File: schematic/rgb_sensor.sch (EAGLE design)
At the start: 6 parts, among them IC2 MEGA8-P

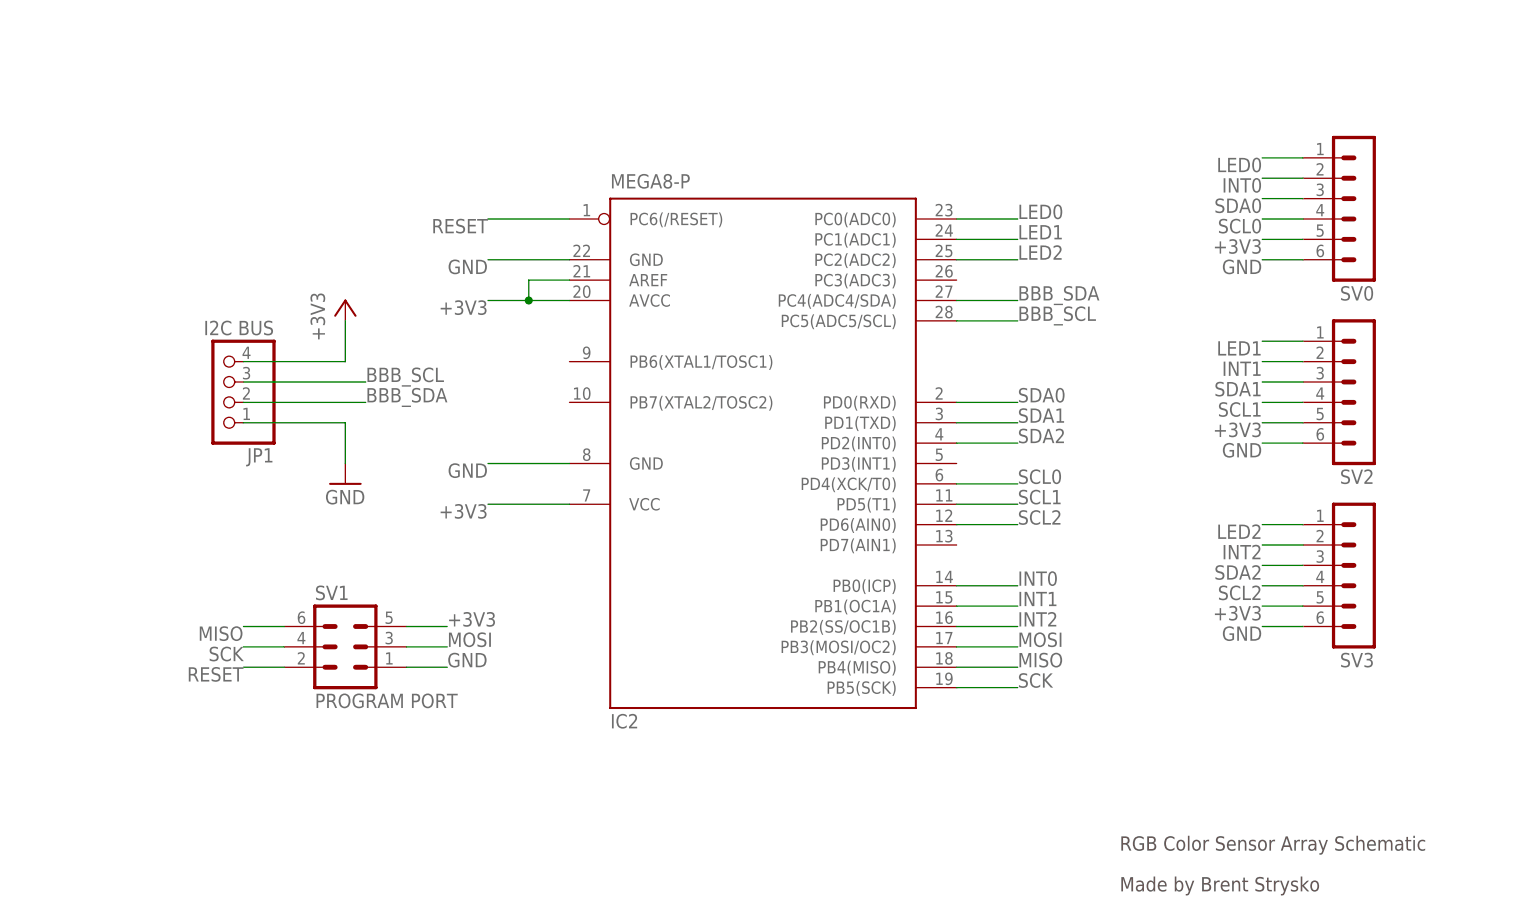
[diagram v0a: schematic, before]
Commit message: Redesigned schematic and board.  Added decoupling capacitors, pullup resistor on reset, and shrunk board size
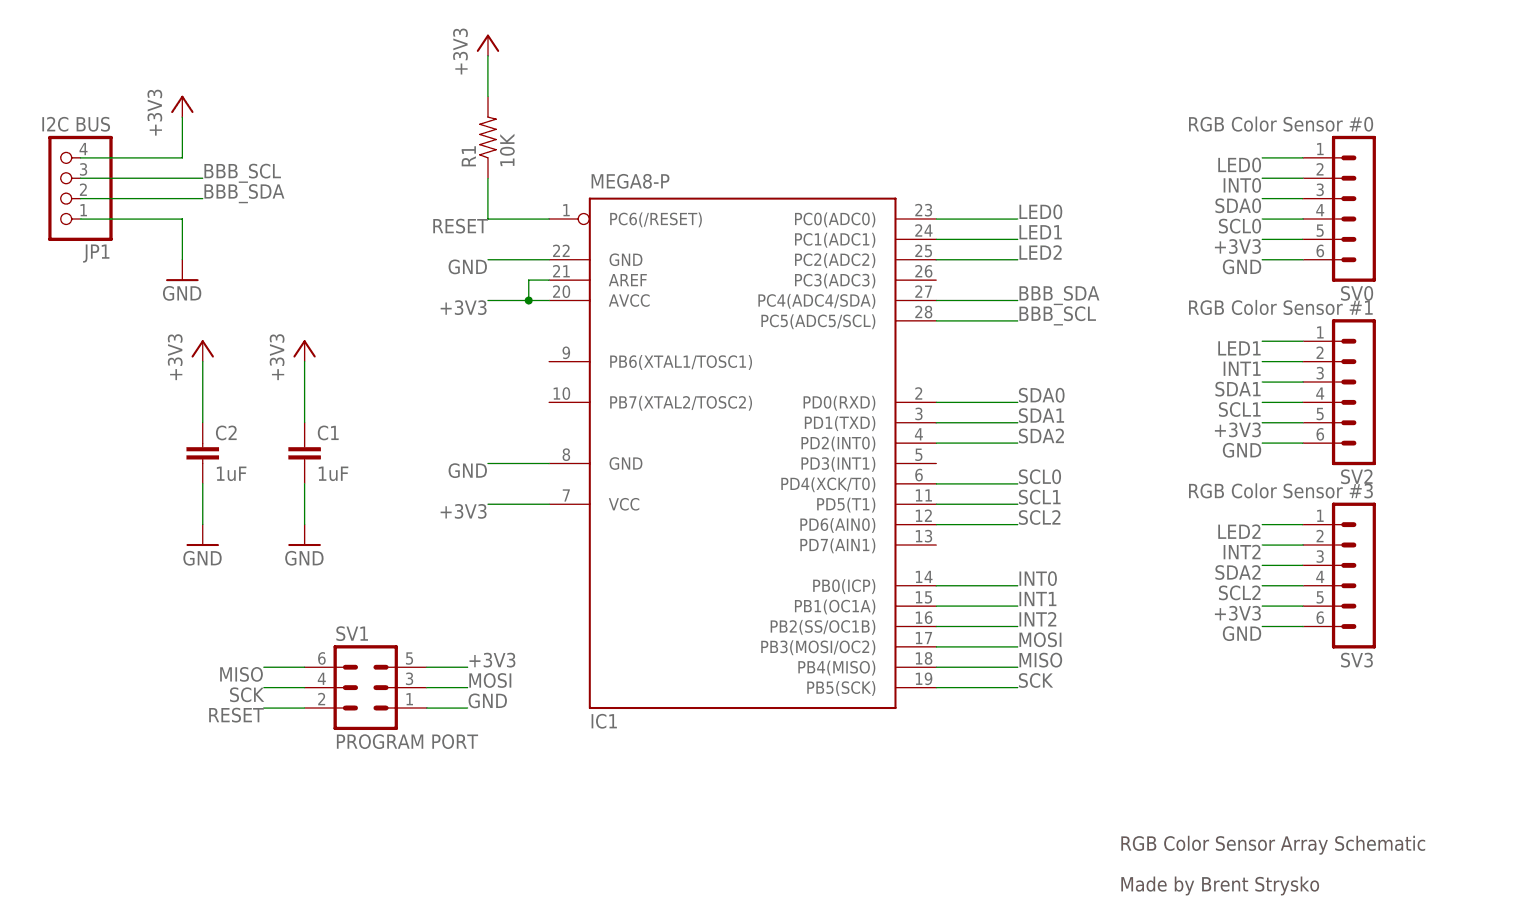
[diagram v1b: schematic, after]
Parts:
- removed IC2: MEGA8-P, atmel:MEGA8-P
- added C1, C2: 1uF, SparkFun-Passives:CAPKIT
- added IC1: MEGA8-P, atmel:MEGA8-P
- added R1: 10K, SparkFun-Passives:RESISTORPTH-1/4W
- SV0: value (none) -> RGB Color Sensor #0
- SV2: value (none) -> RGB Color Sensor #1
- SV3: value (none) -> RGB Color Sensor #3
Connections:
- net +3V3: now also C1.1, C2.1, IC1.AREF, IC1.AVCC, IC1.VCC@1, R1.2; no longer IC2.AREF, IC2.AVCC, IC2.VCC@1
- net BBB_SCL: now also IC1.PC5(ADC5/SCL); no longer IC2.PC5(ADC5/SCL)
- net BBB_SDA: now also IC1.PC4(ADC4/SDA); no longer IC2.PC4(ADC4/SDA)
- net GND: now also C1.2, C2.2, IC1.GND, IC1.GND@1; no longer IC2.GND, IC2.GND@1
- net INT0: now also IC1.PB0(ICP); no longer IC2.PB0(ICP)
- net INT1: now also IC1.PB1(OC1A); no longer IC2.PB1(OC1A)
- net INT2: now also IC1.PB2(SS/OC1B); no longer IC2.PB2(SS/OC1B)
- net LED0: now also IC1.PC0(ADC0); no longer IC2.PC0(ADC0)
- net LED1: now also IC1.PC1(ADC1); no longer IC2.PC1(ADC1)
- net LED2: now also IC1.PC2(ADC2); no longer IC2.PC2(ADC2)
- net MISO: now also IC1.PB4(MISO); no longer IC2.PB4(MISO)
- net MOSI: now also IC1.PB3(MOSI/OC2); no longer IC2.PB3(MOSI/OC2)
- net RESET: now also IC1.PC6(/RESET), R1.1; no longer IC2.PC6(/RESET)
- net SCK: now also IC1.PB5(SCK); no longer IC2.PB5(SCK)
- net SCL0: now also IC1.PD4(XCK/T0); no longer IC2.PD4(XCK/T0)
- net SCL1: now also IC1.PD5(T1); no longer IC2.PD5(T1)
- net SCL2: now also IC1.PD6(AIN0); no longer IC2.PD6(AIN0)
- net SDA0: now also IC1.PD0(RXD); no longer IC2.PD0(RXD)
- net SDA1: now also IC1.PD1(TXD); no longer IC2.PD1(TXD)
- net SDA2: now also IC1.PD2(INT0); no longer IC2.PD2(INT0)
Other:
- moved on the sheet: JP1, SV1
